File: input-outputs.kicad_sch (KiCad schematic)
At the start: 3 parts, among them J5 I2C-STEMMA-QT, J6 UART, J7 Conn_02x05_Odd_Even

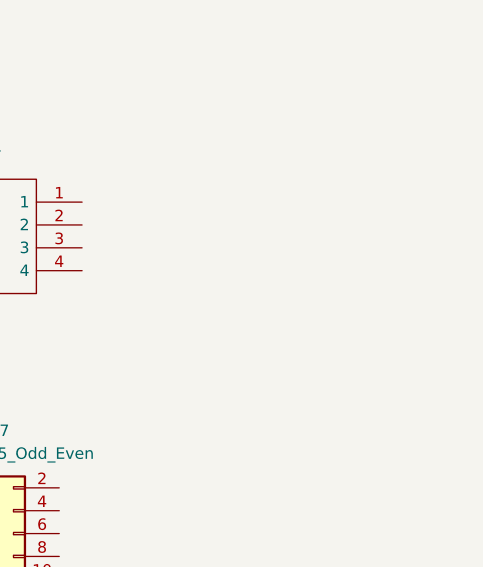
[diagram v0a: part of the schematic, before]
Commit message: Added I2S Audio amplifier
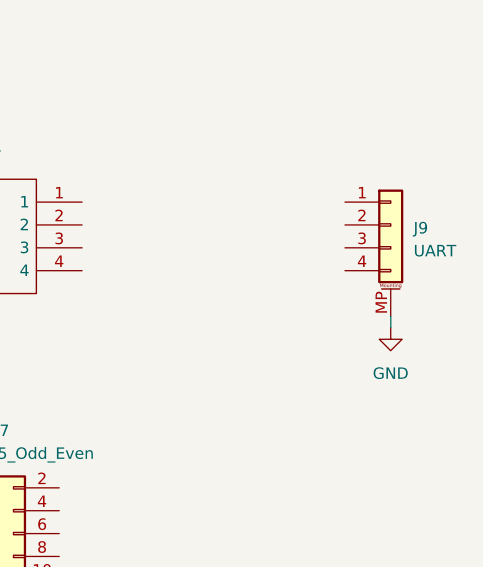
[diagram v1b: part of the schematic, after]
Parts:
- added J9: UART, Connector_Hirose:Hirose_DF13C_CL535-0404-8-51_1x04-1MP_P1.25mm_Vertical, symbol Connector_Generic_MountingPin:Conn_01x04_MountingPin
- J6: footprint KiCad:S4BXHSM4TBLFSN -> (none)
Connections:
- new net GND: J9.MP (MountPin)
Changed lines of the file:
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@@
 	(generator_version "8.0")
 	(paper "A4")
+	(wire
+		(pts
+			(xy 90.17 86.36) (xy 90.17 85.09)
+		)
+		(stroke
+			(width 0)
+			(type default)
+		)
+	)
+	(symbol
+		(lib_id "Connector_Generic_MountingPin:Conn_01x04_MountingPin")
+		(at 90.17 74.93 0)
+		(unit 1)
+		(exclude_from_sim no)
+		(in_bom yes)
+		(on_board yes)
+		(dnp no)
+		(fields_autoplaced yes)
+		(property "Reference" "J9"
+			(at 92.71 75.2855 0)
+			(effects
+				(font
+					(size 1.27 1.27)
+				)
+				(justify left)
+			)
+		)
+		(property "Value" "UART"
+			(at 92.71 77.8255 0)
+			(effects
+				(font
+					(size 1.27 1.27)
+				)
+				(justify left)
+			)
+		)
+		(property "Footprint" "Connector_Hirose:Hirose_DF13C_CL535-0404-8-51_1x04-1MP_P1.25mm_Vertical"
+			(at 90.17 74.93 0)
+			(effects
+				(font
+					(size 1.27 1.27)
+				)
+				(hide yes)
+			)
+		)
+		(property "Datasheet" "~"
+			(at 90.17 74.93 0)
+			(effects
+				(font
+					(size 1.27 1.27)
+				)
+				(hide yes)
+			)
+		)
+		(property "Description" "Generic connectable mounting pin connector, single row, 01x04, script generated (kicad-library-utils/schlib/autogen/connector/)"
+			(at 90.17 74.93 0)
+			(effects
+				(font
+					(size 1.27 1.27)
+				)
+				(hide yes)
+			)
+		)
+		(pin "2"
+		)
+		(pin "1"
+		)
+		(pin "3"
+		)
+		(pin "4"
+		)
+		(pin "MP"
+		)
+		(instances
+			(project "H743_LCD_dev"
+				(path "/70094798-b7e4-48a4-a512-b8f48be18f9f/cf3c6c38-1b0f-4722-9440-d8d8f6f0e2e1"
+					(reference "J9")
+					(unit 1)
+				)
+			)
+		)
+	)
 	(symbol
 		(lib_id "S4B-XH-SM4-TB_LF__SN_:S4B-XH-SM4-TB_LF__SN_")
@@
 			)
 		)
-		(property "Footprint" "KiCad:S4BXHSM4TBLFSN"
+		(property "Footprint" ""
 			(at 52.07 69.85 0)
 			(effects
@@
 					(unit 1)
 				)
+			)
+		)
+	)
+	(symbol
+		(lib_id "power:GND")
+		(at 90.17 86.36 0)
+		(unit 1)
+		(exclude_from_sim no)
+		(in_bom yes)
+		(on_board yes)
+		(dnp no)
+		(fields_autoplaced yes)
+		(property "Reference" "#PWR068"
+			(at 90.17 92.71 0)
+			(effects
+				(font
+					(size 1.27 1.27)
+				)
+				(hide yes)
+			)
+		)
+		(property "Value" "GND"
+			(at 90.17 91.44 0)
+			(effects
+				(font
+					(size 1.27 1.27)
+				)
+			)
+		)
+		(property "Footprint" ""
+			(at 90.17 86.36 0)
+			(effects
+				(font
+					(size 1.27 1.27)
+				)
+				(hide yes)
+			)
+		)
+		(property "Datasheet" ""
+			(at 90.17 86.36 0)
+			(effects
+				(font
+					(size 1.27 1.27)
+				)
+				(hide yes)
+			)
+		)
+		(property "Description" "Power symbol creates a global label with name \"GND\" , ground"
+			(at 90.17 86.36 0)
+			(effects
+				(font
+					(size 1.27 1.27)
+				)
+				(hide yes)
+			)
+		)
+		(pin "1"
+		)
+		(instances
+			(project "H743_LCD_dev"
+				(path "/70094798-b7e4-48a4-a512-b8f48be18f9f/cf3c6c38-1b0f-4722-9440-d8d8f6f0e2e1"
+					(reference "#PWR068")
+					(unit 1)
+				)

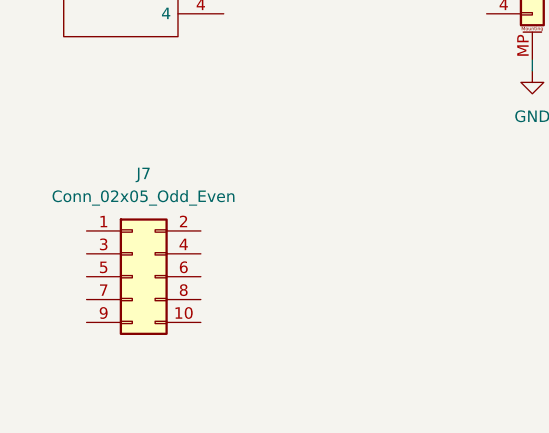
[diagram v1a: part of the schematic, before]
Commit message: Finish sdram, LCD, SD-card, QSPI, I2S tracks
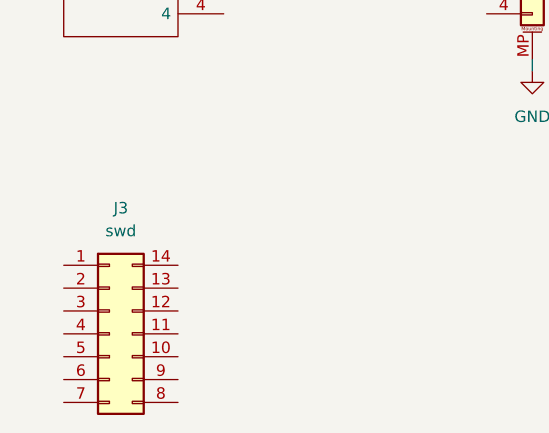
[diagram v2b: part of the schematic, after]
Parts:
- removed J7: Conn_02x05_Odd_Even, Connector_PinHeader_1.27mm:PinHeader_2x05_P1.27mm_Vertical_SMD, symbol Connector_Generic:Conn_02x05_Odd_Even
- added J3: swd, Connector_PinHeader_1.27mm:PinHeader_2x07_P1.27mm_Vertical_SMD, symbol Connector_Generic:Conn_02x07_Counter_Clockwise
- J6: footprint (none) -> SM04B-SRSS-TB_LF__SN_:JST_SM04B-SRSS-TB_LF__SN_
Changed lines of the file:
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@@
+	)
+	(symbol
+		(lib_id "Connector_Generic:Conn_02x07_Counter_Clockwise")
+		(at 43.18 115.57 0)
+		(unit 1)
+		(exclude_from_sim no)
+		(in_bom yes)
+		(on_board yes)
+		(dnp no)
+		(fields_autoplaced yes)
+		(property "Reference" "J3"
+			(at 44.45 101.6 0)
+			(effects
+				(font
+					(size 1.27 1.27)
+				)
+			)
+		)
+		(property "Value" "swd"
+			(at 44.45 104.14 0)
+			(effects
+				(font
+					(size 1.27 1.27)
+				)
+			)
+		)
+		(property "Footprint" "Connector_PinHeader_1.27mm:PinHeader_2x07_P1.27mm_Vertical_SMD"
+			(at 43.18 115.57 0)
+			(effects
+				(font
+					(size 1.27 1.27)
+				)
+				(hide yes)
+			)
+		)
+		(property "Datasheet" "~"
+			(at 43.18 115.57 0)
+			(effects
+				(font
+					(size 1.27 1.27)
+				)
+				(hide yes)
+			)
+		)
+		(property "Description" "Generic connector, double row, 02x07, counter clockwise pin numbering scheme (similar to DIP package numbering), script generated (kicad-library-utils/schlib/autogen/connector/)"
+			(at 43.18 115.57 0)
+			(effects
+				(font
+					(size 1.27 1.27)
+				)
+				(hide yes)
+			)
+		)
+		(pin "9"
+		)
+		(pin "8"
+		)
+		(pin "6"
+		)
+		(pin "5"
+		)
+		(pin "4"
+		)
+		(pin "1"
+		)
+		(pin "12"
+		)
+		(pin "2"
+		)
+		(pin "13"
+		)
+		(pin "14"
+		)
+		(pin "10"
+		)
+		(pin "7"
+		)
+		(pin "11"
+		)
+		(pin "3"
+		)
+		(instances
+			(project "H743_LCD_dev"
+				(path "/70094798-b7e4-48a4-a512-b8f48be18f9f/cf3c6c38-1b0f-4722-9440-d8d8f6f0e2e1"
+					(reference "J3")
+					(unit 1)
+				)
+			)
+		)
 	)
 	(symbol
@@
 			)
 		)
-		(property "Footprint" ""
+		(property "Footprint" "SM04B-SRSS-TB_LF__SN_:JST_SM04B-SRSS-TB_LF__SN_"
 			(at 52.07 69.85 0)
 			(effects
@@
 					(unit 1)
 				)
-			)
-		)
-	)
-	(symbol
-		(lib_id "Connector_Generic:Conn_02x05_Odd_Even")
-		(at 45.72 109.22 0)
-		(unit 1)
-		(exclude_from_sim no)
-		(in_bom yes)
-		(on_board yes)
-		(dnp no)
-		(fields_autoplaced yes)
-		(property "Reference" "J7"
-			(at 46.99 97.79 0)
-			(effects
-				(font
-					(size 1.27 1.27)
-				)
-			)
-		)
-		(property "Value" "Conn_02x05_Odd_Even"
-			(at 46.99 100.33 0)
-			(effects
-				(font
-					(size 1.27 1.27)
-				)
-			)
-		)
-		(property "Footprint" "Connector_PinHeader_1.27mm:PinHeader_2x05_P1.27mm_Vertical_SMD"
-			(at 45.72 109.22 0)
-			(effects
-				(font
-					(size 1.27 1.27)
-				)
-				(hide yes)
-			)
-		)
-		(property "Datasheet" "~"
-			(at 45.72 109.22 0)
-			(effects
-				(font
-					(size 1.27 1.27)
-				)
-				(hide yes)
-			)
-		)
-		(property "Description" "Generic connector, double row, 02x05, odd/even pin numbering scheme (row 1 odd numbers, row 2 even numbers), script generated (kicad-library-utils/schlib/autogen/connector/)"
-			(at 45.72 109.22 0)
-			(effects
-				(font
-					(size 1.27 1.27)
-				)
-				(hide yes)
-			)
-		)
-		(pin "9"
-		)
-		(pin "7"
-		)
-		(pin "8"
-		)
-		(pin "1"
-		)
-		(pin "3"
-		)
-		(pin "10"
-		)
-		(pin "5"
-		)
-		(pin "4"
-		)
-		(pin "6"
-		)
-		(pin "2"
-		)
-		(instances
-			(project "H743_LCD_dev"
-				(path "/70094798-b7e4-48a4-a512-b8f48be18f9f/cf3c6c38-1b0f-4722-9440-d8d8f6f0e2e1"
-					(reference "J7")
-					(unit 1)
-				)

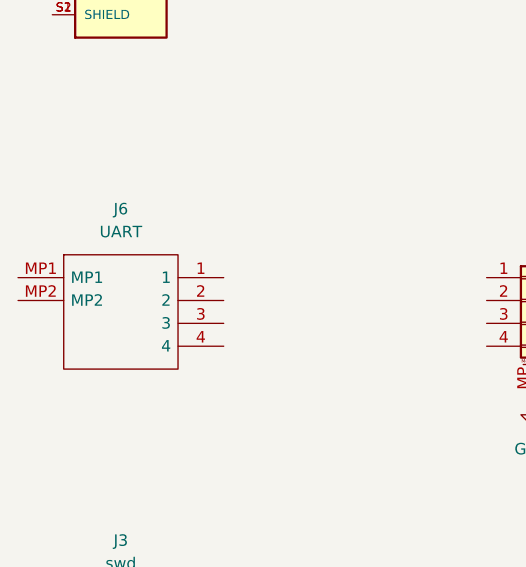
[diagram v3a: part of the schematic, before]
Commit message: Changed the FPC footprint and uart, added RTC battery connector
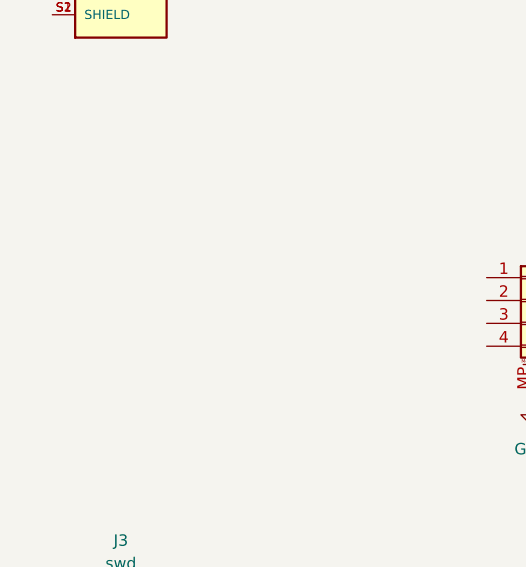
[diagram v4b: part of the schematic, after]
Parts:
- removed J6: UART, SM04B-SRSS-TB_LF__SN_:JST_SM04B-SRSS-TB_LF__SN_, symbol S4B-XH-SM4-TB_LF__SN_:S4B-XH-SM4-TB_LF__SN_
- J3: JLCPCB Part # (none) -> C2881912
- J5: JLCPCB Part # (none) -> C160404
- J9: footprint Connector_Hirose:Hirose_DF13C_CL535-0404-8-51_1x04-1MP_P1.25mm_Vertical -> S4B-XH-SM4-TB_LF__SN:S4BXHSM4TBLFSN; JLCPCB Part # (none) -> C146120
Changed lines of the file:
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@@
 			)
 		)
-		(property "JLCPCB Part #" ""
+		(property "JLCPCB Part #" "C2881912"
+			(at 43.18 115.57 0)
+			(effects
+				(font
+					(size 1.27 1.27)
+				)
+				(hide yes)
+			)
+		)
+		(property "Arrow Part Number" ""
+			(at 43.18 115.57 0)
+			(effects
+				(font
+					(size 1.27 1.27)
+				)
+				(hide yes)
+			)
+		)
+		(property "Arrow Price/Stock" ""
+			(at 43.18 115.57 0)
+			(effects
+				(font
+					(size 1.27 1.27)
+				)
+				(hide yes)
+			)
+		)
+		(property "Height" ""
+			(at 43.18 115.57 0)
+			(effects
+				(font
+					(size 1.27 1.27)
+				)
+				(hide yes)
+			)
+		)
+		(property "Manufacturer_Name" ""
+			(at 43.18 115.57 0)
+			(effects
+				(font
+					(size 1.27 1.27)
+				)
+				(hide yes)
+			)
+		)
+		(property "Manufacturer_Part_Number" ""
+			(at 43.18 115.57 0)
+			(effects
+				(font
+					(size 1.27 1.27)
+				)
+				(hide yes)
+			)
+		)
+		(property "Mouser Part Number" ""
+			(at 43.18 115.57 0)
+			(effects
+				(font
+					(size 1.27 1.27)
+				)
+				(hide yes)
+			)
+		)
+		(property "Mouser Price/Stock" ""
 			(at 43.18 115.57 0)
 			(effects
@@
 			)
 		)
-		(property "Footprint" "Connector_Hirose:Hirose_DF13C_CL535-0404-8-51_1x04-1MP_P1.25mm_Vertical"
+		(property "Footprint" "S4B-XH-SM4-TB_LF__SN:S4BXHSM4TBLFSN"
 			(at 90.17 74.93 0)
 			(effects
@@
 			)
 		)
-		(property "JLCPCB Part #" ""
+		(property "JLCPCB Part #" "C146120"
+			(at 90.17 74.93 0)
+			(effects
+				(font
+					(size 1.27 1.27)
+				)
+				(hide yes)
+			)
+		)
+		(property "Arrow Part Number" ""
+			(at 90.17 74.93 0)
+			(effects
+				(font
+					(size 1.27 1.27)
+				)
+				(hide yes)
+			)
+		)
+		(property "Arrow Price/Stock" ""
+			(at 90.17 74.93 0)
+			(effects
+				(font
+					(size 1.27 1.27)
+				)
+				(hide yes)
+			)
+		)
+		(property "Height" ""
+			(at 90.17 74.93 0)
+			(effects
+				(font
+					(size 1.27 1.27)
+				)
+				(hide yes)
+			)
+		)
+		(property "Manufacturer_Name" ""
+			(at 90.17 74.93 0)
+			(effects
+				(font
+					(size 1.27 1.27)
+				)
+				(hide yes)
+			)
+		)
+		(property "Manufacturer_Part_Number" ""
+			(at 90.17 74.93 0)
+			(effects
+				(font
+					(size 1.27 1.27)
+				)
+				(hide yes)
+			)
+		)
+		(property "Mouser Part Number" ""
+			(at 90.17 74.93 0)
+			(effects
+				(font
+					(size 1.27 1.27)
+				)
+				(hide yes)
+			)
+		)
+		(property "Mouser Price/Stock" ""
 			(at 90.17 74.93 0)
 			(effects
@@
 				(path "/70094798-b7e4-48a4-a512-b8f48be18f9f/cf3c6c38-1b0f-4722-9440-d8d8f6f0e2e1"
 					(reference "J9")
-					(unit 1)
-				)
-			)
-		)
-	)
-	(symbol
-		(lib_id "S4B-XH-SM4-TB_LF__SN_:S4B-XH-SM4-TB_LF__SN_")
-		(at 33.02 72.39 0)
-		(unit 1)
-		(exclude_from_sim no)
-		(in_bom yes)
-		(on_board yes)
-		(dnp no)
-		(fields_autoplaced yes)
-		(property "Reference" "J6"
-			(at 44.45 64.77 0)
-			(effects
-				(font
-					(size 1.27 1.27)
-				)
-			)
-		)
-		(property "Value" "UART"
-			(at 44.45 67.31 0)
-			(effects
-				(font
-					(size 1.27 1.27)
-				)
-			)
-		)
-		(property "Footprint" "SM04B-SRSS-TB_LF__SN_:JST_SM04B-SRSS-TB_LF__SN_"
-			(at 52.07 69.85 0)
-			(effects
-				(font
-					(size 1.27 1.27)
-				)
-				(justify left)
-				(hide yes)
-			)
-		)
-		(property "Datasheet" "https://datasheet.lcsc.com/szlcsc/JST-Sales-America-XHsocket-1-4P-SMD-pitch2-5mm_C161861.pdf"
-			(at 52.07 72.39 0)
-			(effects
-				(font
-					(size 1.27 1.27)
-				)
-				(justify left)
-				(hide yes)
-			)
-		)
-		(property "Description" "Conn Shrouded Header HDR 4 POS 2.5mm Solder RA SMD T/R"
-			(at 52.07 74.93 0)
-			(effects
-				(font
-					(size 1.27 1.27)
-				)
-				(justify left)
-				(hide yes)
-			)
-		)
-		(property "Height" "6"
-			(at 52.07 77.47 0)
-			(effects
-				(font
-					(size 1.27 1.27)
-				)
-				(justify left)
-				(hide yes)
-			)
-		)
-		(property "Manufacturer_Name" "JST (JAPAN SOLDERLESS TERMINALS)"
-			(at 52.07 80.01 0)
-			(effects
-				(font
-					(size 1.27 1.27)
-				)
-				(justify left)
-				(hide yes)
-			)
-		)
-		(property "Manufacturer_Part_Number" "S4B-XH-SM4-TB(LF)(SN)"
-			(at 52.07 82.55 0)
-			(effects
-				(font
-					(size 1.27 1.27)
-				)
-				(justify left)
-				(hide yes)
-			)
-		)
-		(property "Mouser Part Number" ""
-			(at 52.07 85.09 0)
-			(effects
-				(font
-					(size 1.27 1.27)
-				)
-				(justify left)
-				(hide yes)
-			)
-		)
-		(property "Mouser Price/Stock" ""
-			(at 52.07 87.63 0)
-			(effects
-				(font
-					(size 1.27 1.27)
-				)
-				(justify left)
-				(hide yes)
-			)
-		)
-		(property "Arrow Part Number" "S4B-XH-SM4-TB(LF)(SN)"
-			(at 52.07 90.17 0)
-			(effects
-				(font
-					(size 1.27 1.27)
-				)
-				(justify left)
-				(hide yes)
-			)
-		)
-		(property "Arrow Price/Stock" "https://www.arrow.com/en/products/s4b-xh-sm4-tb-lf-sn/jst-manufacturing"
-			(at 52.07 92.71 0)
-			(effects
-				(font
-					(size 1.27 1.27)
-				)
-				(justify left)
-				(hide yes)
-			)
-		)
-		(property "JLCPCB Part #" ""
-			(at 33.02 72.39 0)
-			(effects
-				(font
-					(size 1.27 1.27)
-				)
-				(hide yes)
-			)
-		)
-		(pin "3"
-		)
-		(pin "1"
-		)
-		(pin "MP1"
-		)
-		(pin "2"
-		)
-		(pin "MP2"
-		)
-		(pin "4"
-		)
-		(instances
-			(project "H743_LCD_dev"
-				(path "/70094798-b7e4-48a4-a512-b8f48be18f9f/cf3c6c38-1b0f-4722-9440-d8d8f6f0e2e1"
-					(reference "J6")
 					(unit 1)
 				)
@@
 			)
 		)
-		(property "JLCPCB Part #" ""
-			(at 44.45 35.56 0)
-			(effects
+		(property "JLCPCB Part #" "C160404"
+			(at 44.45 35.56 0)
+			(effects
+				(font
+					(size 1.27 1.27)
+				)
+				(hide yes)
+			)
+		)
+		(property "Arrow Part Number" ""
+			(at 44.45 35.56 0)
+			(effects
+				(font
+					(size 1.27 1.27)
+				)
+				(hide yes)
+			)
+		)
+		(property "Arrow Price/Stock" ""
+			(at 44.45 35.56 0)
+			(effects
+				(font
+					(size 1.27 1.27)
+				)
+				(hide yes)
+			)
+		)
+		(property "Height" ""
+			(at 44.45 35.56 0)
+			(effects
+				(font
+					(size 1.27 1.27)
+				)
+				(hide yes)
+			)
+		)
+		(property "Manufacturer_Name" ""
+			(at 44.45 35.56 0)
+			(effects
+				(font
+					(size 1.27 1.27)
+				)
+				(hide yes)
+			)
+		)
+		(property "Manufacturer_Part_Number" ""
+			(at 44.45 35.56 0)
+			(effects
+				(font
+					(size 1.27 1.27)
+				)
+				(hide yes)
+			)
+		)
+		(property "Mouser Part Number" ""
+			(at 44.45 35.56 0)
+			(effects
+				(font
+					(size 1.27 1.27)
+				)
+				(hide yes)
+			)
+		)
+		(property "Mouser Price/Stock" ""
+			(at 44.45 35.56 0)
+			(effects

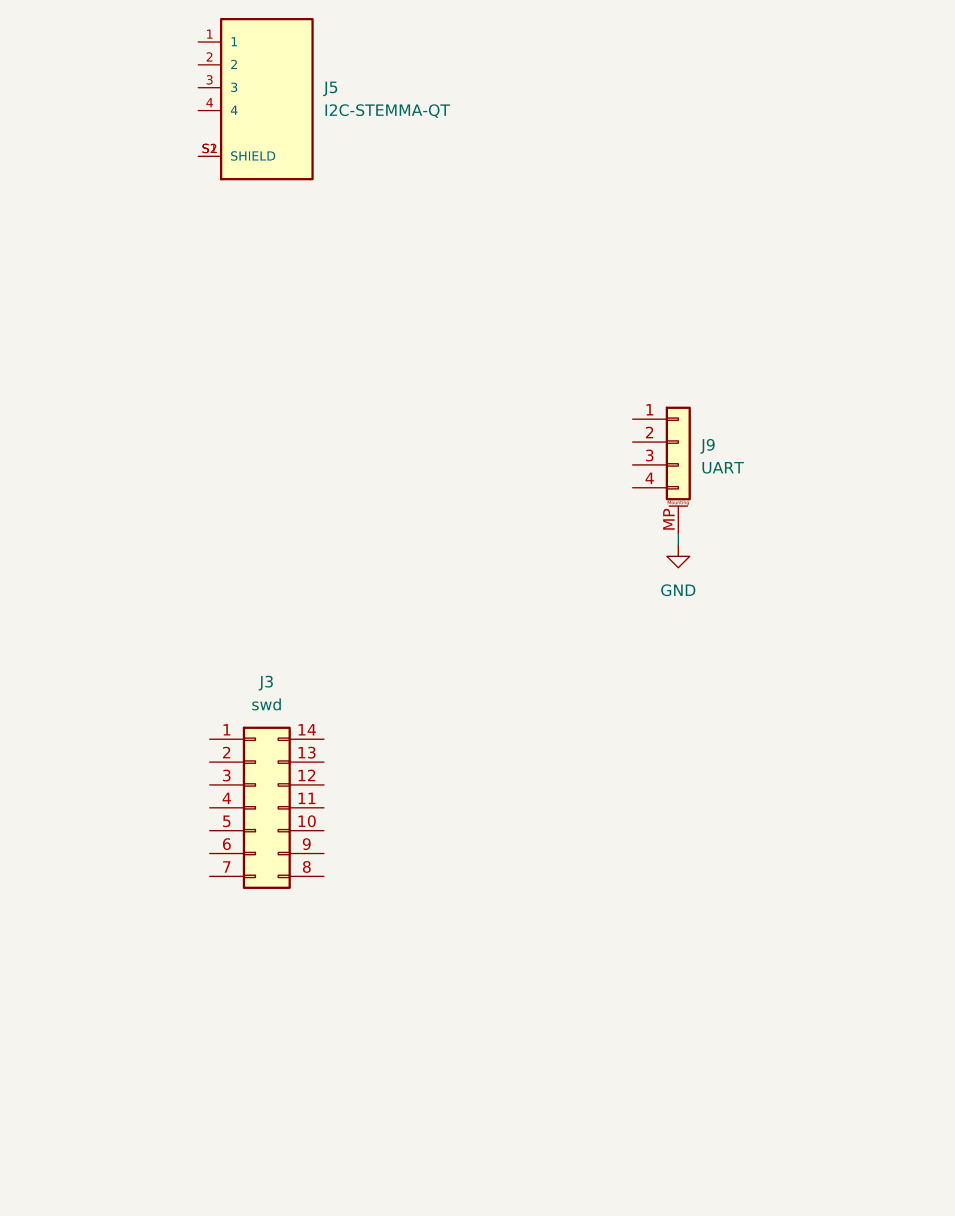
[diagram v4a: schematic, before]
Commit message: Added UART esd
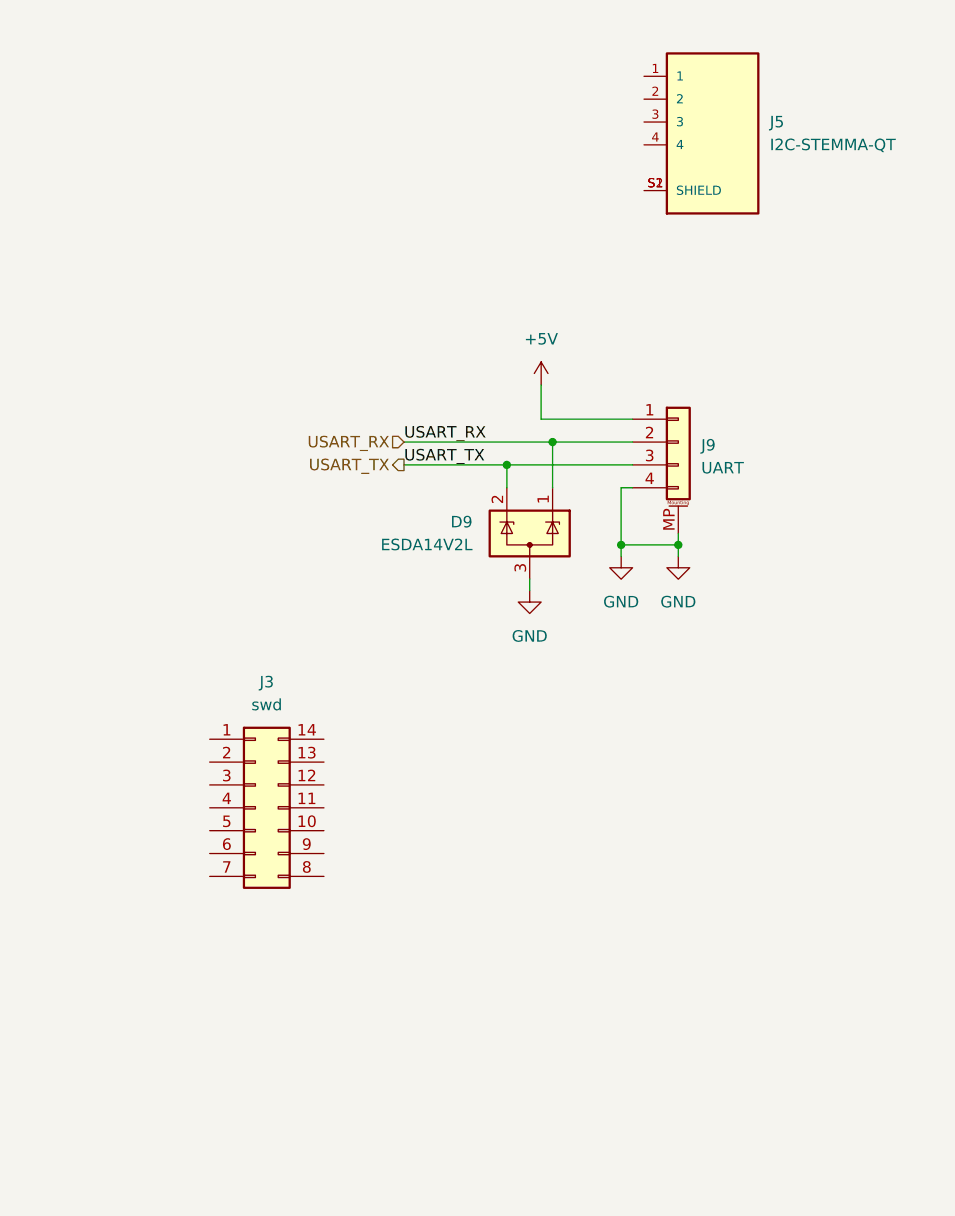
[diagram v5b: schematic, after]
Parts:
- added D9: ESDA14V2L, Package_TO_SOT_SMD:SOT-23, symbol Power_Protection:SP0502BAHT
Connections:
- net GND: now also J9.4 (Pin_4), D9.3 (A)
- net +5V: now reaches J9.1 (Pin_1)
- net USART_RX: now reaches J9.2 (Pin_2)
- net USART_RX: now also D9.1 (K)
- net USART_TX: now reaches J9.3 (Pin_3)
- net USART_TX: now also D9.2 (K)
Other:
- moved on the sheet: J5
